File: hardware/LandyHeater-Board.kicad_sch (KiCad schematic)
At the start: 0 parts

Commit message: Complete phase 2 schematic review
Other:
- added sheet AUTOTERM UART and 1-Wire (05_AUTOTERM_1Wire.kicad_sch)
- added sheet E-paper power and interface (03_Display_EPaper.kicad_sch)
- added sheet ESP32-S3, native USB, reset and boot (02_ESP32_USB_Reset.kicad_sch)
- added sheet External controls, lighting and diagnostics (06_Controls_Diagnostics.kicad_sch)
- added sheet Power input, USB-C and 3.3 V (01_Power_Input_USB.kicad_sch)
- added sheet Touch always-on rail and RTC (04_Touch_RTC.kicad_sch)
- title: Landy Heater Controller -> Landy Heater Controller - Hierarchy
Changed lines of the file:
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@@
-(kicad_sch
-	(version 20250114)
-	(generator "eeschema")
-	(generator_version "9.0")
-	(paper "A4")
-	(title_block
-		(title "Landy Heater Controller")
-		(date "2026-09-06")
-		(rev "A")
-		(company "LandyHeater")
-		(comment 1 "Phase 0 project scaffold - not released for production")
-		(comment 2 "ESP32-S3-WROOM-1U-N16R8")
-	)
-	(sheet_instances
-		(path "/"
-			(page "1")
-		)
-	)
-	(embedded_fonts no)
+(kicad_sch (version 20250114) (generator eeschema)
+  (paper "A4")
+  (title_block
+    (title "Landy Heater Controller - Hierarchy")
+    (date "2026-09-06")
+    (rev "A / Phase 2")
+    (company "LandyHeater")
+    (comment 1 "Review schematic - NOT RELEASED FOR PRODUCTION")
+    (comment 2 "ESP32-S3-WROOM-1U-N16R8 / 10-14V vehicle auxiliary battery / USB-C")
+  )
+  (sheet (at 25.40 35.56) (size 76.20 30.48) (fields_autoplaced)
+    (exclude_from_sim no) (in_bom yes) (on_board yes) (dnp no)
+    (stroke (width 0) (type solid) (color 0 0 0 0))
+    (fill (color 0 0 0 0.0000))
+    (property "Sheet name" "Power input, USB-C and 3.3 V" (id 0) (at 25.40 34.72 0) (effects (font (size 1.27 1.27)) (justify left bottom)))
+    (property "Sheet file" "01_Power_Input_USB.kicad_sch" (id 1) (at 25.40 66.88 0) (effects (font (size 1.27 1.27)) (justify left top)))
+    (instances
+      (project "LandyHeater-Board"
+        (path "/fc880c51-6059-52cc-a5eb-c6da339cdcce" (page "2"))
+      )
+    )
+  )
+  (sheet (at 120.65 35.56) (size 76.20 30.48) (fields_autoplaced)
+    (exclude_from_sim no) (in_bom yes) (on_board yes) (dnp no)
+    (stroke (width 0) (type solid) (color 0 0 0 0))
+    (fill (color 0 0 0 0.0000))
+    (property "Sheet name" "ESP32-S3, native USB, reset and boot" (id 0) (at 120.65 34.72 0) (effects (font (size 1.27 1.27)) (justify left bottom)))
+    (property "Sheet file" "02_ESP32_USB_Reset.kicad_sch" (id 1) (at 120.65 66.88 0) (effects (font (size 1.27 1.27)) (justify left top)))
+    (instances
+      (project "LandyHeater-Board"
+        (path "/fc880c51-6059-52cc-a5eb-c6da339cdcce" (page "3"))
+      )
+    )
+  )
+  (sheet (at 25.40 86.36) (size 76.20 30.48) (fields_autoplaced)
+    (exclude_from_sim no) (in_bom yes) (on_board yes) (dnp no)
+    (stroke (width 0) (type solid) (color 0 0 0 0))
+    (fill (color 0 0 0 0.0000))
+    (property "Sheet name" "E-paper power and interface" (id 0) (at 25.40 85.52 0) (effects (font (size 1.27 1.27)) (justify left bottom)))
+    (property "Sheet file" "03_Display_EPaper.kicad_sch" (id 1) (at 25.40 117.68 0) (effects (font (size 1.27 1.27)) (justify left top)))
+    (instances
+      (project "LandyHeater-Board"
+        (path "/fc880c51-6059-52cc-a5eb-c6da339cdcce" (page "4"))
+      )
+    )
+  )
+  (sheet (at 120.65 86.36) (size 76.20 30.48) (fields_autoplaced)
+    (exclude_from_sim no) (in_bom yes) (on_board yes) (dnp no)
+    (stroke (width 0) (type solid) (color 0 0 0 0))
+    (fill (color 0 0 0 0.0000))
+    (property "Sheet name" "Touch always-on rail and RTC" (id 0) (at 120.65 85.52 0) (effects (font (size 1.27 1.27)) (justify left bottom)))
+    (property "Sheet file" "04_Touch_RTC.kicad_sch" (id 1) (at 120.65 117.68 0) (effects (font (size 1.27 1.27)) (justify left top)))
+    (instances
+      (project "LandyHeater-Board"
+        (path "/fc880c51-6059-52cc-a5eb-c6da339cdcce" (page "5"))
+      )
+    )
+  )
+  (sheet (at 25.40 137.16) (size 76.20 30.48) (fields_autoplaced)
+    (exclude_from_sim no) (in_bom yes) (on_board yes) (dnp no)
+    (stroke (width 0) (type solid) (color 0 0 0 0))
+    (fill (color 0 0 0 0.0000))
+    (property "Sheet name" "AUTOTERM UART and 1-Wire" (id 0) (at 25.40 136.32 0) (effects (font (size 1.27 1.27)) (justify left bottom)))
+    (property "Sheet file" "05_AUTOTERM_1Wire.kicad_sch" (id 1) (at 25.40 168.48 0) (effects (font (size 1.27 1.27)) (justify left top)))
+    (instances
+      (project "LandyHeater-Board"
+        (path "/fc880c51-6059-52cc-a5eb-c6da339cdcce" (page "6"))
+      )
+    )
+  )
+  (sheet (at 120.65 137.16) (size 76.20 30.48) (fields_autoplaced)
+    (exclude_from_sim no) (in_bom yes) (on_board yes) (dnp no)
+    (stroke (width 0) (type solid) (color 0 0 0 0))
+    (fill (color 0 0 0 0.0000))
+    (property "Sheet name" "External controls, lighting and diagnostics" (id 0) (at 120.65 136.32 0) (effects (font (size 1.27 1.27)) (justify left bottom)))
+    (property "Sheet file" "06_Controls_Diagnostics.kicad_sch" (id 1) (at 120.65 168.48 0) (effects (font (size 1.27 1.27)) (justify left top)))
+    (instances
+      (project "LandyHeater-Board"
+        (path "/fc880c51-6059-52cc-a5eb-c6da339cdcce" (page "7"))
+      )
+    )
+  )
+  (sheet_instances
+    (path "/" (page "1"))
+  )
 )

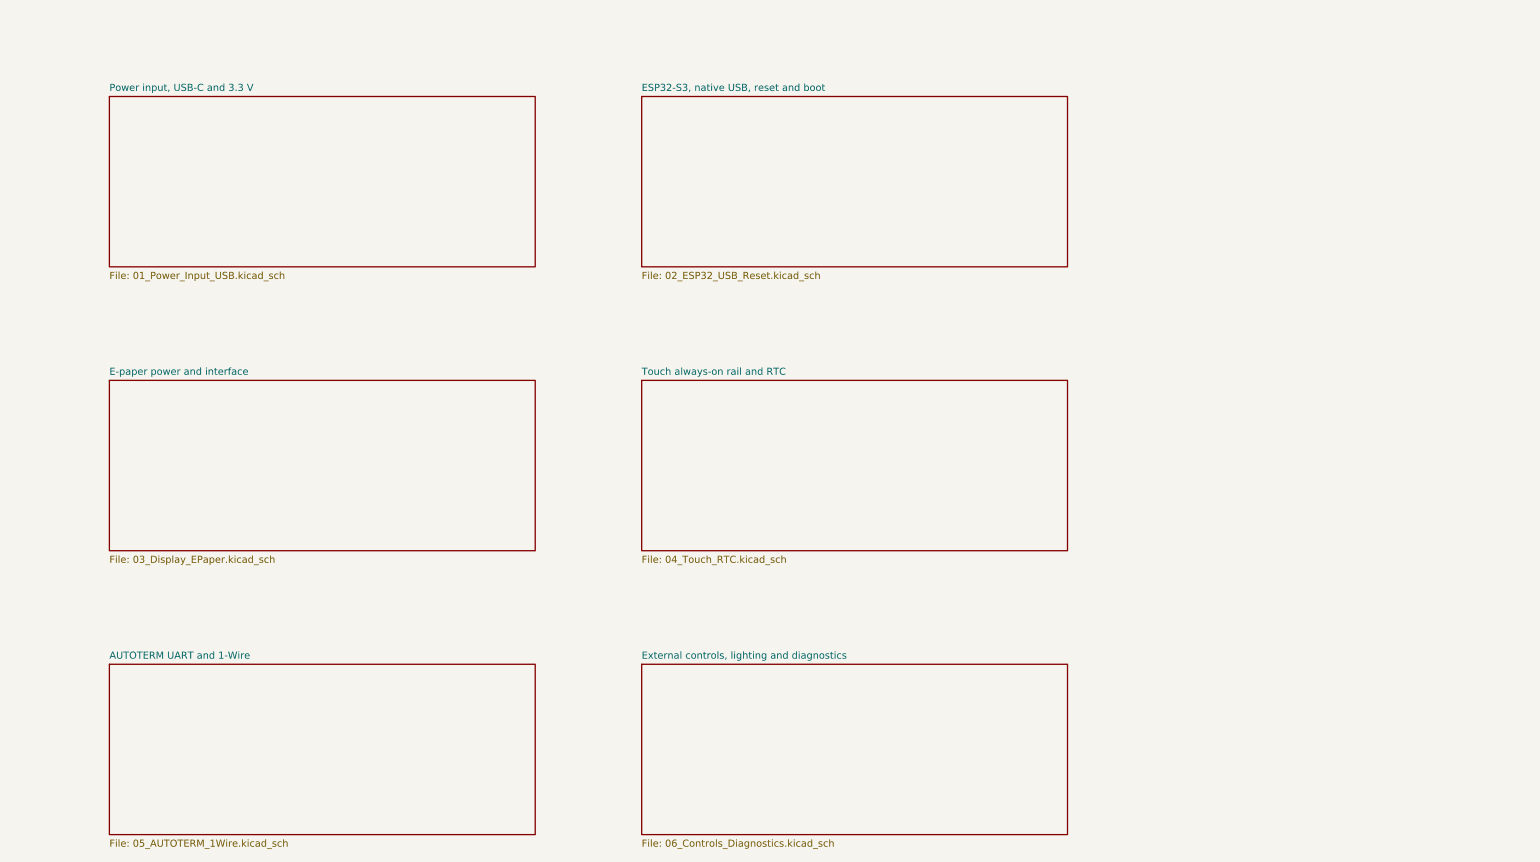
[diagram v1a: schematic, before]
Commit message: Redraw phase 2 schematic with visible functional wiring
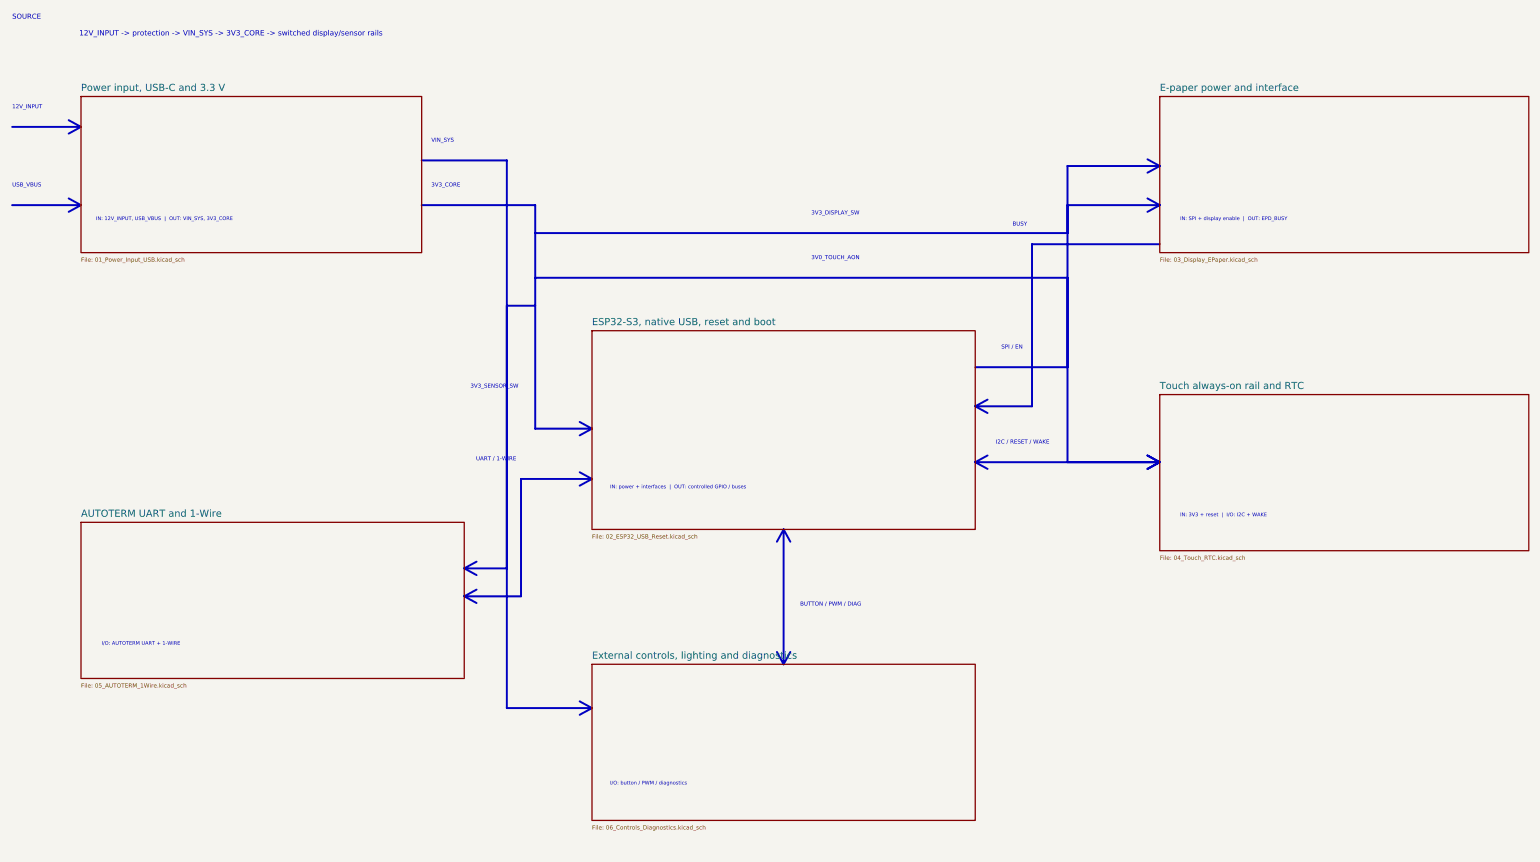
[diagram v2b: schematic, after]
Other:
- note added: "12V_INPUT"
- note added: "12V_INPUT -> protection -> VIN_SYS -> 3V3_CORE -> switched display/sensor rails"
- note added: "3V0_TOUCH_AON"
- note added: "3V3_CORE"
- note added: "3V3_DISPLAY_SW"
- note added: "3V3_SENSOR_SW"
- note added: "BUSY"
- note added: "BUTTON / PWM / DIAG"
- note added: "I/O: AUTOTERM UART + 1-WIRE"
- note added: "I/O: button / PWM / diagnostics"
- note added: "I2C / RESET / WAKE"
- note added: "IN: 12V_INPUT, USB_VBUS | OUT: VIN_SYS, 3V3_CORE"
- note added: "IN: 3V3 + reset | I/O: I2C + WAKE"
- note added: "IN: SPI + display enable | OUT: EPD_BUSY"
- note added: "IN: power + interfaces | OUT: controlled GPIO / buses"
- note added: "SOURCE"
- note added: "SPI / EN"
- note added: "UART / 1-WIRE"
- note added: "USB_VBUS"
- note added: "VIN_SYS"
- title: Landy Heater Controller - Hierarchy -> Landy Heater Controller - System Architecture
